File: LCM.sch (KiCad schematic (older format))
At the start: 17 parts, among them J5 3-84952-0, J6 F52R-1A7H1-11020

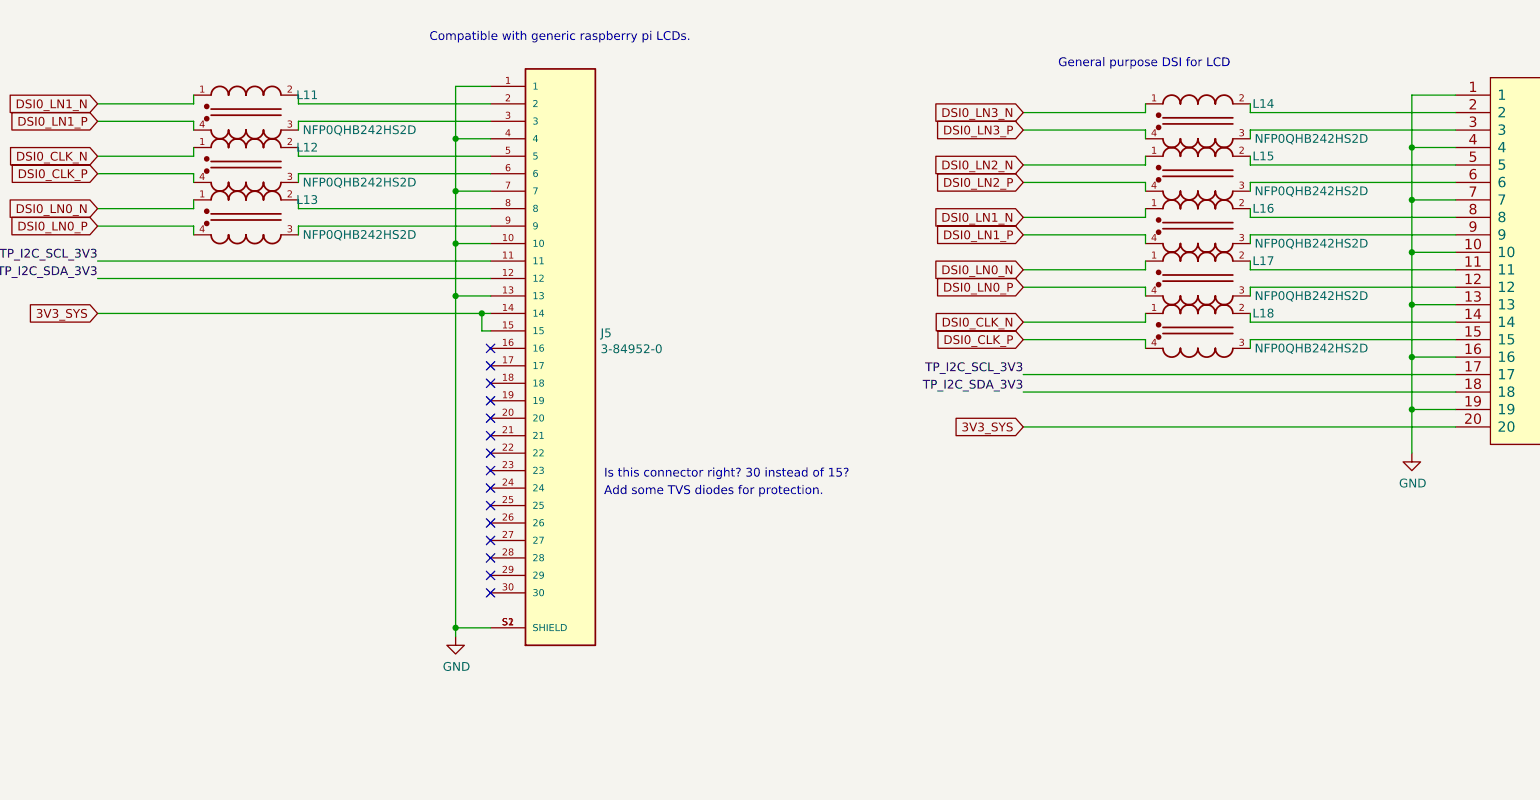
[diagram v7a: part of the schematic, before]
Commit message: Change 30pin connector to 15 pin one
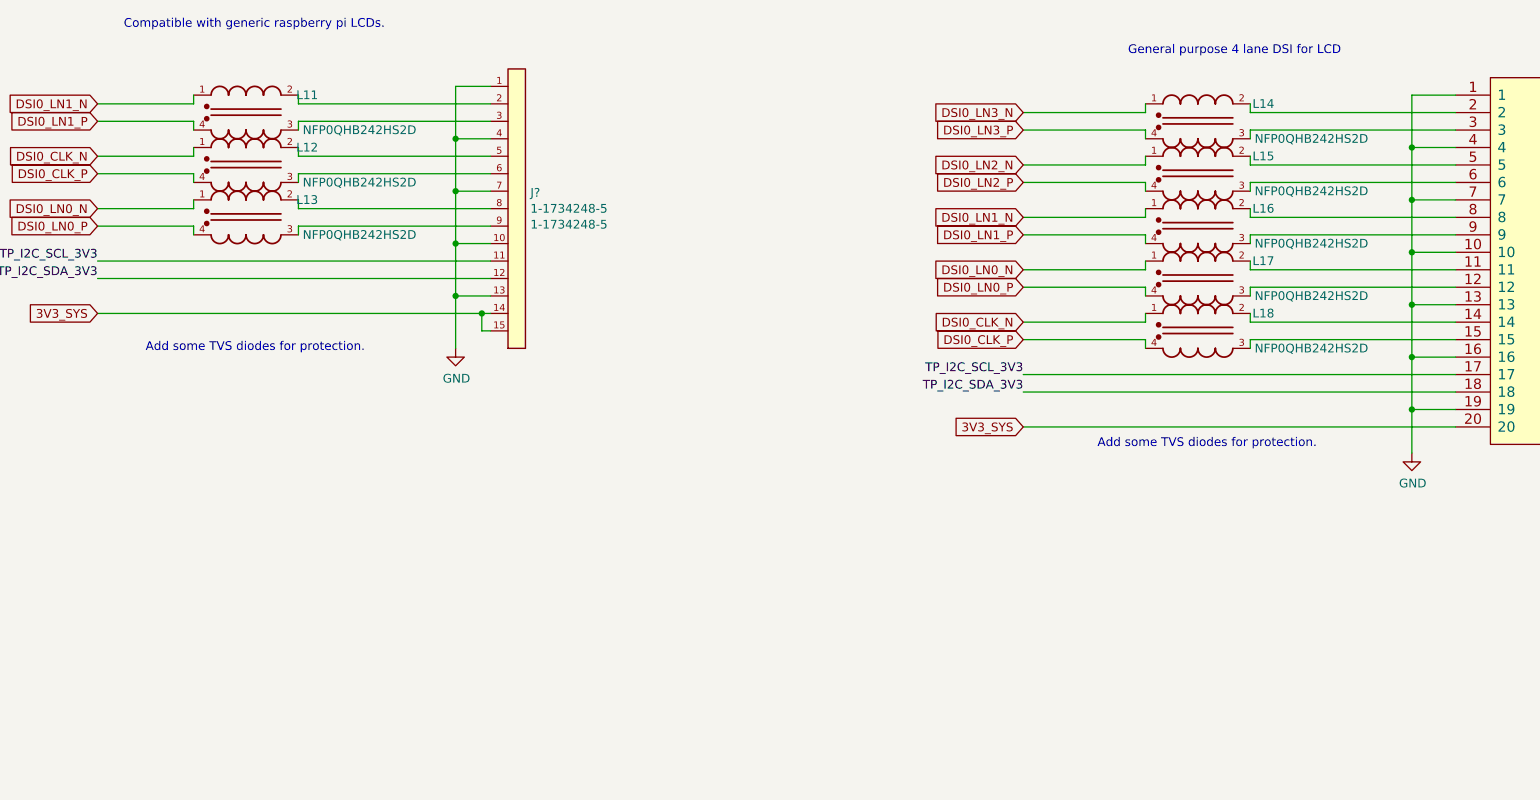
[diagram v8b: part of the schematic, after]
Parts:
- removed J5: 3-84952-0, sa800u-baseboard-hw-footprints:TE_3-84952-0, symbol sa800u-baseboard-hw:3-84952-0
- added J?: 1-1734248-5, antmicro-footprints:TE_1-1734248-5, symbol antmicroFCCConnectors:1-1734248-5
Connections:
- net 3V3_SYS: now also J?.14, J?.15
- net GND: now also J?.1, J?.10, J?.13, J?.4, J?.7
- net TP_I2C_SCL_3V3: now also J?.11
- net TP_I2C_SDA_3V3: now also J?.12
- net at L11.2: now also J?.2
- net at L11.3: now also J?.3
- net at L12.2: now also J?.5
- net at L12.3: now also J?.6
- net at L13.2: now also J?.8
- net at L13.3: now also J?.9
- no-connect marks 15 -> 0
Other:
- note added: "General purpose 4 lane DSI for LCD"
- note removed: "General purpose DSI for LCD"
- note removed: "Is this connector right? 30 instead of 15?\n"
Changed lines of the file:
@@
 Wire Wire Line
 	4925 4150 2725 4150
-Wire Wire Line
-	4775 4050 4775 5950
 Connection ~ 4775 4050
 $Comp
 L sa800u-baseboard-hw:GND #PWR063
 U 1 1 61BD6C0B
-P 4775 6000
-F 0 "#PWR063" H 4775 5750 50  0001 C CNN
-F 1 "GND" H 4780 5827 50  0000 C CNN
-F 2 "" H 4775 6000 50  0001 C CNN
-F 3 "" H 4775 6000 50  0001 C CNN
-	1    4775 6000
+P 4775 4350
+F 0 "#PWR063" H 4775 4100 50  0001 C CNN
+F 1 "GND" H 4780 4177 50  0000 C CNN
+F 2 "" H 4775 4350 50  0001 C CNN
+F 3 "" H 4775 4350 50  0001 C CNN
+	1    4775 4350
 	1    0    0    -1
 $EndComp
@@
 Wire Wire Line
 	9325 4350 9325 4300
-$Comp
-L sa800u-baseboard-hw:3-84952-0 J5
-U 1 1 619D8F59
-P 5375 4250
-F 0 "J5" H 5605 4237 50  0000 L CNN
-F 1 "3-84952-0" H 5605 4146 50  0000 L CNN
-F 2 "sa800u-baseboard-hw-footprints:TE_3-84952-0" H 6175 4150 50  0001 L BNN
-F 3 "https://www.te.com/commerce/DocumentDelivery/DDEController?Action=showdoc&DocId=Data+Sheet%7F1-1773959-6-flexible-printed-circuit-con%7F0919%7Fpdf%7FEnglish%7FENG_DS_1-1773959-6-flexible-printed-circuit-con_0919.pdf%7F3-84952-0" H 6175 4150 50  0001 L BNN
-F 4 "3-84952-0" H 5605 4055 50  0001 L CNN "MPN"
-F 5 "AMP - TE CONNECTIVITY" H 5605 3964 50  0001 L CNN "Manufacturer"
-	1    5375 4250
-	1    0    0    -1
-$EndComp
-NoConn ~ 4975 4350
-NoConn ~ 4975 4450
-NoConn ~ 4975 4550
-NoConn ~ 4975 4650
-NoConn ~ 4975 4750
-NoConn ~ 4975 4850
-NoConn ~ 4975 4950
-NoConn ~ 4975 5050
-NoConn ~ 4975 5150
-NoConn ~ 4975 5250
-NoConn ~ 4975 5350
-NoConn ~ 4975 5450
-NoConn ~ 4975 5550
-NoConn ~ 4975 5650
-NoConn ~ 4975 5750
-Text Notes 4625 2600 0    50   ~ 0
+Text Notes 2875 2525 0    50   ~ 0
 Compatible with generic raspberry pi LCDs.
-Text Notes 5625 5100 0    50   ~ 0
-Is this connector right? 30 instead of 15?\n
-Text Notes 8225 2750 0    50   ~ 0
-General purpose DSI for LCD
+Text Notes 8625 2675 0    50   ~ 0
+General purpose 4 lane DSI for LCD
 $Comp
 L sa800u-baseboard-hw:F52R-1A7H1-11020 J6
@@
 Text GLabel 8025 4800 0    50   Input ~ 0
 3V3_SYS
-Text Notes 5625 5200 0    50   ~ 0
+Text Notes 3000 4375 0    50   ~ 0
 Add some TVS diodes for protection.
 $Comp
@@
 Wire Wire Line
 	8025 4600 10500 4600
-Wire Wire Line
-	4775 5950 4975 5950
-Connection ~ 4775 5950
-Wire Wire Line
-	4775 5950 4775 6000
 Connection ~ 4925 4150
+$Comp
+L antmicroFCCConnectors:1-1734248-5 J?
+U 1 1 66288CCF
+P 5125 3550
+F 0 "J?" H 5203 3641 50  0000 L CNN
+F 1 "1-1734248-5" H 5203 3550 50  0000 L CNN
+F 2 "antmicro-footprints:TE_1-1734248-5" H 4675 2250 50  0001 L BNN
+F 3 "https://www.te.com/commerce/DocumentDelivery/DDEController?Action=showdoc&DocId=Customer+Drawing%7F1734248%7FE1%7Fpdf%7FEnglish%7FENG_CD_1734248_E1__.pdf%7F1-1734248-5" H 5275 3550 50  0001 L BNN
+F 4 "TE Connectivity " H 4675 2350 50  0001 L BNN "Manufacturer"
+F 5 "1-1734248-5 " H 5203 3459 50  0000 L CNN "MPN"
+	1    5125 3550
+	1    0    0    -1
+$EndComp
+Wire Wire Line
+	4775 4050 4775 4350
+Text Notes 8450 4925 0    50   ~ 0
+Add some TVS diodes for protection.
 $EndSCHEMATC
